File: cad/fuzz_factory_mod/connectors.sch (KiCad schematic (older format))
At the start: 12 parts, among them J1701 Barrel_Jack_Switch, J1702 Conn_Battery, J1703 CONN_AUDIO_OUT, J1704 CONN_AUDIO_IN, K1701 EE2-5NU, Q1701 DTC114Y, Q1702 DTA114E

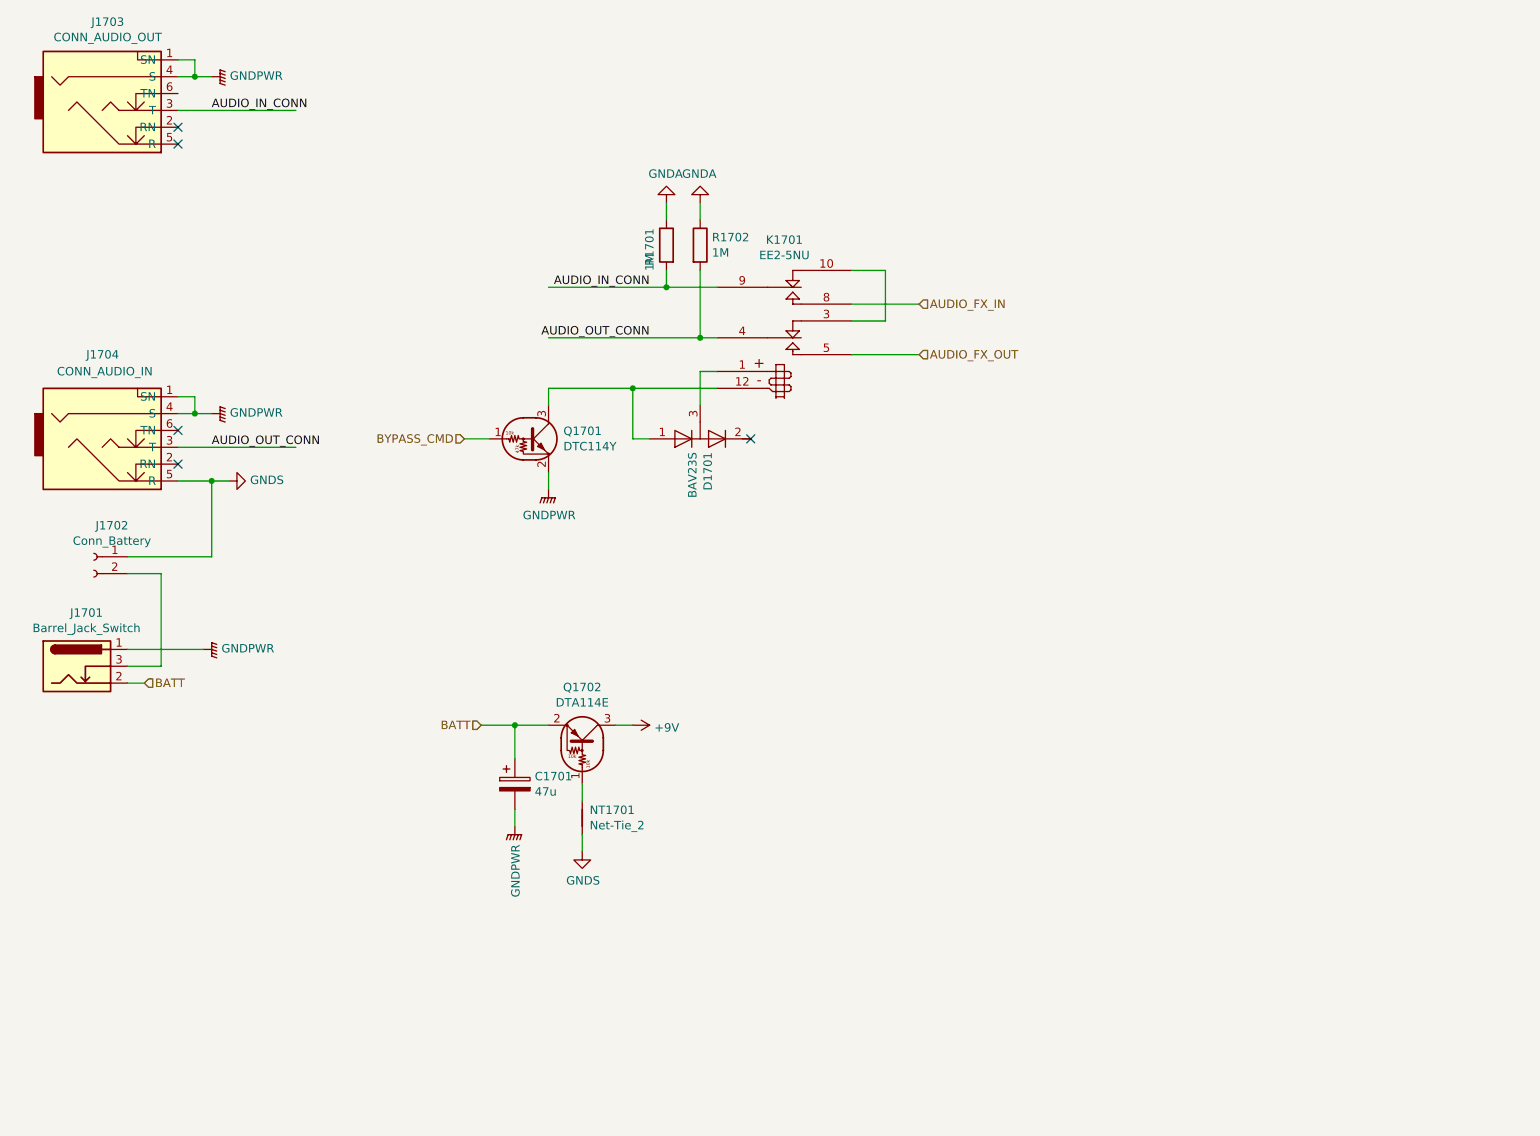
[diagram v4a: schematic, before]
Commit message: Continued schematic.
Continued component placement.
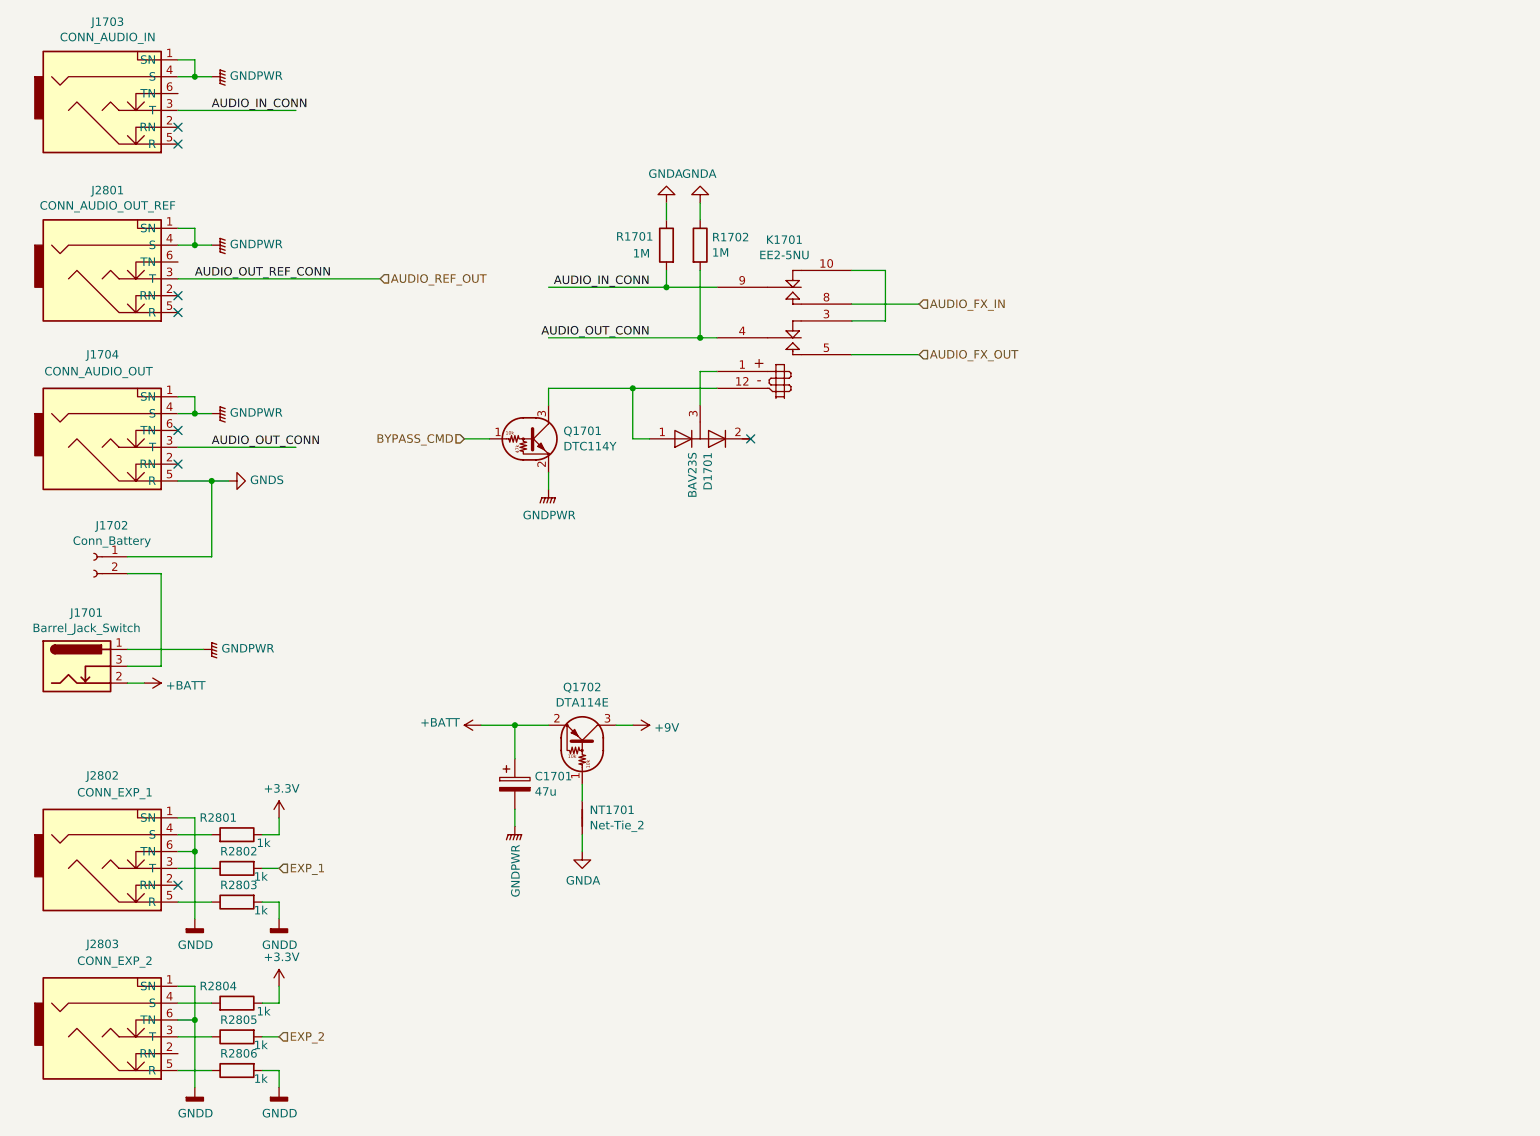
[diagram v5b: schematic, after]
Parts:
- added J2801: CONN_AUDIO_OUT_REF, Connect:NMJ6HCD2, symbol flax_lib:CLIFF_FCR50051
- added J2802: CONN_EXP_1, Connect:NMJ6HCD2, symbol flax_lib:CLIFF_FCR50051
- added J2803: CONN_EXP_2, Connect:NMJ6HCD2, symbol flax_lib:CLIFF_FCR50051
- added R2801, R2802, R2803, R2804, R2805, R2806: 1k, Resistors_SMD:R_0603, symbol Device:R
- J1703: value CONN_AUDIO_OUT -> CONN_AUDIO_IN
- J1704: value CONN_AUDIO_IN -> CONN_AUDIO_OUT
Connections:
- net labels added: +3.3V, +BATT, AUDIO_OUT_REF_CONN, AUDIO_REF_OUT, EXP_1, EXP_2, GNDD
- net labels removed: BATT
- wire segments 48 -> 77
- no-connect marks 5 -> 8
